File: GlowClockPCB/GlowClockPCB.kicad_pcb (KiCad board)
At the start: 2 copper layers, 102.9 x 64.8 mm, 30 parts, among them J1 LED_OUT_1, J2 LED_OUT_2, J3 LED_OUT_3, J4 LED_OUT_4, J5 POWER_IN, U1 RaspberryPi_Pico_W, U2 Raspberry_Pi_Zero_2_W, U3 DS3231MZ

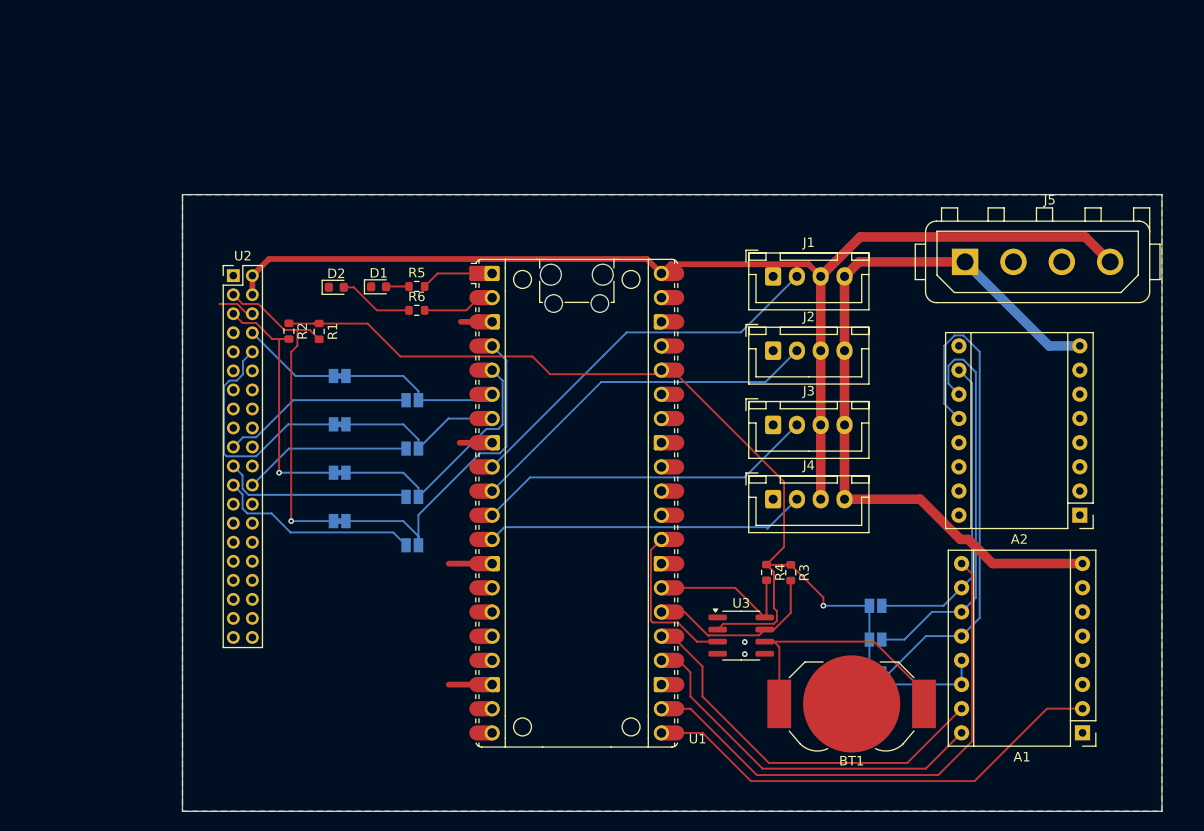
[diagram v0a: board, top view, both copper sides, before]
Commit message: add output connectors for motor drivers
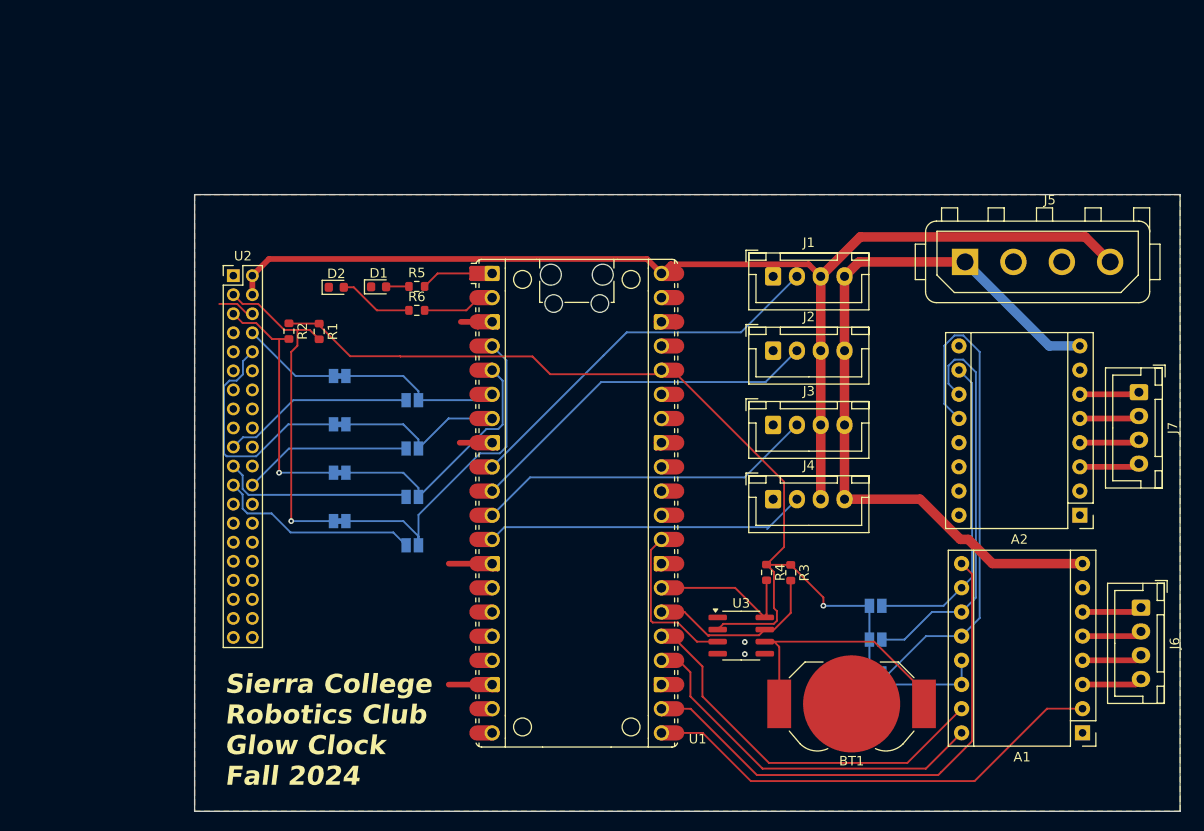
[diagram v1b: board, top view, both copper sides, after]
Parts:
- added J6: Motor_1_Out, Connector_JST:JST_XH_B4B-XH-A_1x04_P2.50mm_Vertical, F.Cu at (173.1, 156.4)
- added J7: Motor_2_Out, Connector_JST:JST_XH_B4B-XH-A_1x04_P2.50mm_Vertical, F.Cu at (172.8, 133.8)
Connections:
- A1 pad 3: unconnected-(A1-A2-Pad3) -> Net-(A1-A2)
- A1 pad 4: unconnected-(A1-A1-Pad4) -> Net-(A1-A1)
- A1 pad 5: unconnected-(A1-B1-Pad5) -> Net-(A1-B1)
- A1 pad 6: unconnected-(A1-B2-Pad6) -> Net-(A1-B2)
- A2 pad 3: unconnected-(A2-A2-Pad3) -> Net-(A2-A2)
- A2 pad 4: unconnected-(A2-A1-Pad4) -> Net-(A2-A1)
- A2 pad 5: unconnected-(A2-B1-Pad5) -> Net-(A2-B1)
- A2 pad 6: unconnected-(A2-B2-Pad6) -> Net-(A2-B2)
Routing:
- net Net-(A1-A2): track 0.00 -> 6.38 mm
- net Net-(A1-A1): track 0.00 -> 6.36 mm
- net Net-(A2-A2): track 0.00 -> 6.34 mm
- net Net-(A1-B1): track 0.00 -> 6.34 mm
- net Net-(A2-A1): track 0.00 -> 6.33 mm
- net Net-(A1-B2): track 0.00 -> 6.33 mm
- net Net-(A2-B1): track 0.00 -> 6.31 mm
- net Net-(A2-B2): track 0.00 -> 6.29 mm
- net +3V3: track 115.7 -> 115.2 mm
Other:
- board size 102.9 x 64.8 mm -> 103.5 x 64.8 mm
- board text added: "Sierra College Robotics Club Glow Clock Fall 2024"

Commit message: thicken high-current traces, and move text from silkscreen to copper layer
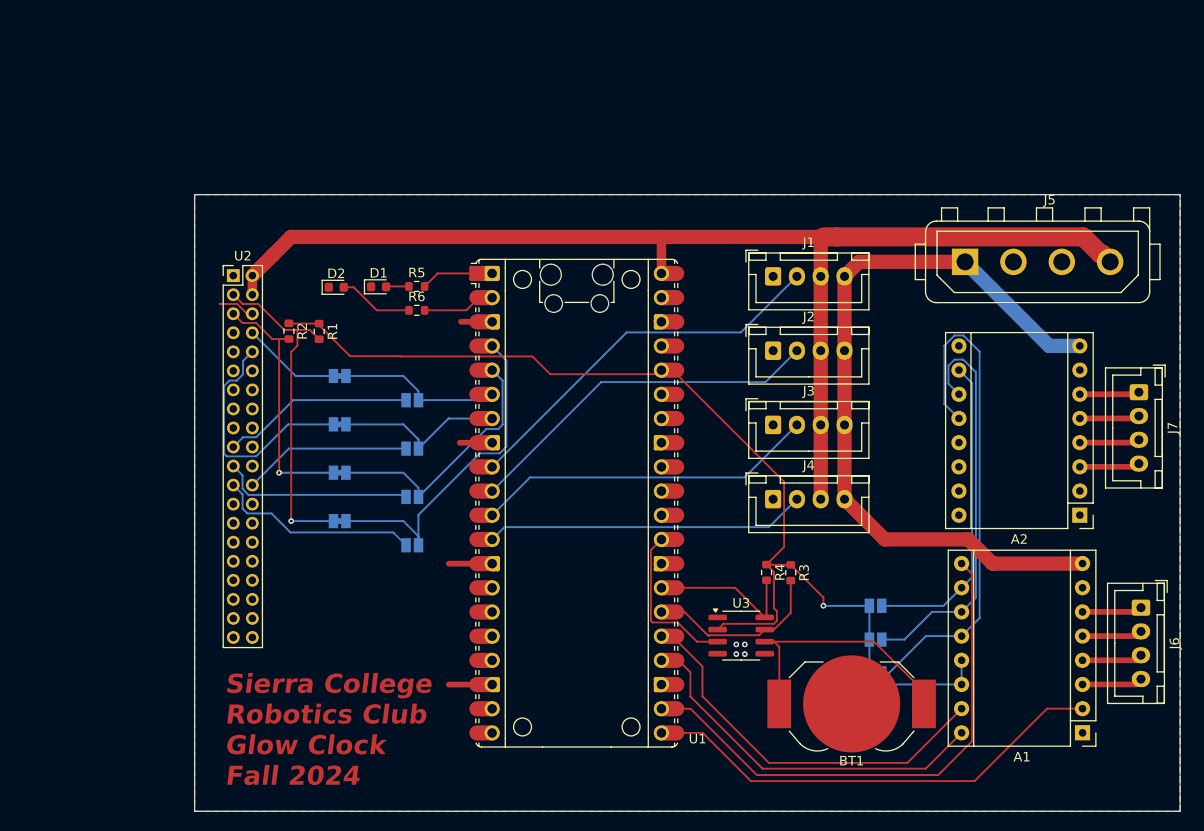
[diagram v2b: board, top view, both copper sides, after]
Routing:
- net +5V: track 120.6 -> 126.4 mm
- net GND: vias 2 -> 4
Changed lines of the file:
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@@
 		)
 		(property "Value" "StepperMode2"
-			(at 0 -1.9 0)
+			(at 0 -1.646 0)
 			(layer "B.SilkS")
 			(effects
@@
 	(gr_text "Sierra College\nRobotics Club\nGlow Clock\nFall 2024"
 		(at 76.835 175.26 0)
-		(layer "F.SilkS")
+		(layer "F.Cu")
+		(effects
+			(font
+				(size 2 2)
+				(thickness 0.3)
+				(bold yes)
+				(italic yes)
+			)
+			(justify left bottom)
+		)
+	)
+	(gr_text "Sierra College\nRobotics Club\nGlow Clock\nFall 2024"
+		(at 76.835 175.26 0)
+		(layer "F.Mask")
 		(effects
 			(font
@@
 	)
 	(via
-		(at 131.445 160.02)
+		(at 131.445 160.274)
+		(size 0.6)
+		(drill 0.3)
+		(layers "F.Cu" "B.Cu")
+		(free yes)
+		(net 1)
+	)
+	(via
+		(at 130.556 160.274)
+		(size 0.6)
+		(drill 0.3)
+		(layers "F.Cu" "B.Cu")
+		(free yes)
+		(net 1)
+	)
+	(via
+		(at 130.556 161.29)
 		(size 0.6)
 		(drill 0.3)
@@
 	)
 	(segment
-		(start 79.725 121.54)
-		(end 79.725 123.54)
-		(width 0.6)
+		(start 139.7 117.475)
+		(end 122.555 117.475)
+		(width 1.5)
 		(layer "F.Cu")
 		(net 17)
 	)
 	(segment
-		(start 122.69 121.31)
-		(end 121.17 119.79)
-		(width 0.6)
+		(start 169.0075 119.2825)
+		(end 168.8125 119.2825)
+		(width 2)
 		(layer "F.Cu")
 		(net 17)
 	)
 	(segment
-		(start 169.82 120.095)
-		(end 167.2 117.475)
+		(start 79.725 123.54)
+		(end 79.725 121.54)
 		(width 1)
 		(layer "F.Cu")
@@
 	)
 	(segment
-		(start 81.475 119.79)
-		(end 79.725 121.54)
-		(width 0.6)
+		(start 168.8125 119.2825)
+		(end 167.005 117.475)
+		(width 2)
 		(layer "F.Cu")
 		(net 17)
 	)
 	(segment
-		(start 138.145 120.345)
-		(end 123.655 120.345)
-		(width 0.6)
+		(start 139.42 117.755)
+		(end 139.7 117.475)
+		(width 1.5)
 		(layer "F.Cu")
 		(net 17)
 	)
 	(segment
-		(start 143.565 117.475)
-		(end 139.42 121.62)
+		(start 83.79 117.475)
+		(end 81.885 119.38)
+		(width 1.5)
+		(layer "F.Cu")
+		(net 17)
+	)
+	(segment
+		(start 141.09 117.475)
+		(end 139.7 117.475)
+		(width 2)
+		(layer "F.Cu")
+		(net 17)
+	)
+	(segment
+		(start 122.69 117.61)
+		(end 122.555 117.475)
 		(width 1)
-		(layer "F.Cu")
-		(net 17)
-	)
-	(segment
-		(start 139.42 121.62)
-		(end 138.145 120.345)
-		(width 0.6)
 		(layer "F.Cu")
 		(net 17)
@@
 		(start 139.42 121.62)
 		(end 139.42 145.02)
+		(width 1.5)
+		(layer "F.Cu")
+		(net 17)
+	)
+	(segment
+		(start 81.885 119.38)
+		(end 79.725 121.54)
+		(width 1.5)
+		(layer "F.Cu")
+		(net 17)
+	)
+	(segment
+		(start 139.42 121.62)
+		(end 139.42 117.755)
+		(width 1.5)
+		(layer "F.Cu")
+		(net 17)
+	)
+	(segment
+		(start 167.005 117.475)
+		(end 141.09 117.475)
+		(width 2)
+		(layer "F.Cu")
+		(net 17)
+	)
+	(segment
+		(start 122.69 121.31)
+		(end 122.69 117.61)
 		(width 1)
 		(layer "F.Cu")
@@
 	)
 	(segment
-		(start 123.655 120.345)
-		(end 122.69 121.31)
-		(width 0.6)
+		(start 169.82 120.095)
+		(end 169.0075 119.2825)
+		(width 2)
 		(layer "F.Cu")
 		(net 17)
 	)
 	(segment
-		(start 121.17 119.79)
-		(end 81.475 119.79)
-		(width 0.6)
-		(layer "F.Cu")
-		(net 17)
-	)
-	(segment
-		(start 167.2 117.475)
-		(end 143.565 117.475)
-		(width 1)
+		(start 122.555 117.475)
+		(end 83.79 117.475)
+		(width 1.5)
 		(layer "F.Cu")
 		(net 17)
@@
 	)
 	(segment
-		(start 141.92 145.02)
-		(end 149.86 145.02)
-		(width 1)
-		(layer "F.Cu")
-		(net 74)
-	)
-	(segment
 		(start 143.445 120.095)
 		(end 141.92 121.62)
-		(width 1)
+		(width 1.5)
 		(layer "F.Cu")
 		(net 74)
 	)
 	(segment
+		(start 166.915 151.78)
+		(end 157.459365 151.78)
+		(width 1.5)
+		(layer "F.Cu")
+		(net 74)
+	)
+	(segment
+		(start 146.142818 149.242818)
+		(end 141.92 145.02)
+		(width 1.5)
+		(layer "F.Cu")
+		(net 74)
+	)
+	(segment
 		(start 154.922182 149.242818)
-		(end 157.459365 151.78)
-		(width 1)
-		(layer "F.Cu")
-		(net 74)
-	)
-	(segment
-		(start 154.082818 149.242818)
-		(end 154.922182 149.242818)
-		(width 1)
+		(end 146.142818 149.242818)
+		(width 1.5)
 		(layer "F.Cu")
 		(net 74)
@@
 		(start 141.92 121.62)
 		(end 141.92 145.02)
-		(width 1)
+		(width 1.5)
 		(layer "F.Cu")
 		(net 74)
@@
 		(start 154.58 120.095)
 		(end 143.445 120.095)
-		(width 1)
+		(width 1.5)
 		(layer "F.Cu")
 		(net 74)
 	)
 	(segment
-		(start 149.86 145.02)
-		(end 154.082818 149.242818)
-		(width 1)
-		(layer "F.Cu")
-		(net 74)
-	)
-	(segment
 		(start 157.459365 151.78)
-		(end 166.915 151.78)
-		(width 1)
+		(end 154.922182 149.242818)
+		(width 1.5)
 		(layer "F.Cu")
 		(net 74)
@@
 		(start 154.58 120.095)
 		(end 163.405 128.92)
-		(width 1)
+		(width 1.5)
 		(layer "B.Cu")
 		(net 74)
@@
 		(start 163.405 128.92)
 		(end 166.635 128.92)
-		(width 1)
+		(width 1.5)
 		(layer "B.Cu")
 		(net 74)
@@
 		(width 0.2)
 		(layer "B.Cu")
-		(net 76)
-	)
-	(segment
-		(start 133.79 148.15)
-		(end 133.985 147.955)
-		(width 0.2)
-		(layer "B.Cu")

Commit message: lots of tweaks to design, add display port, mounting holes, decoupling caps, etc
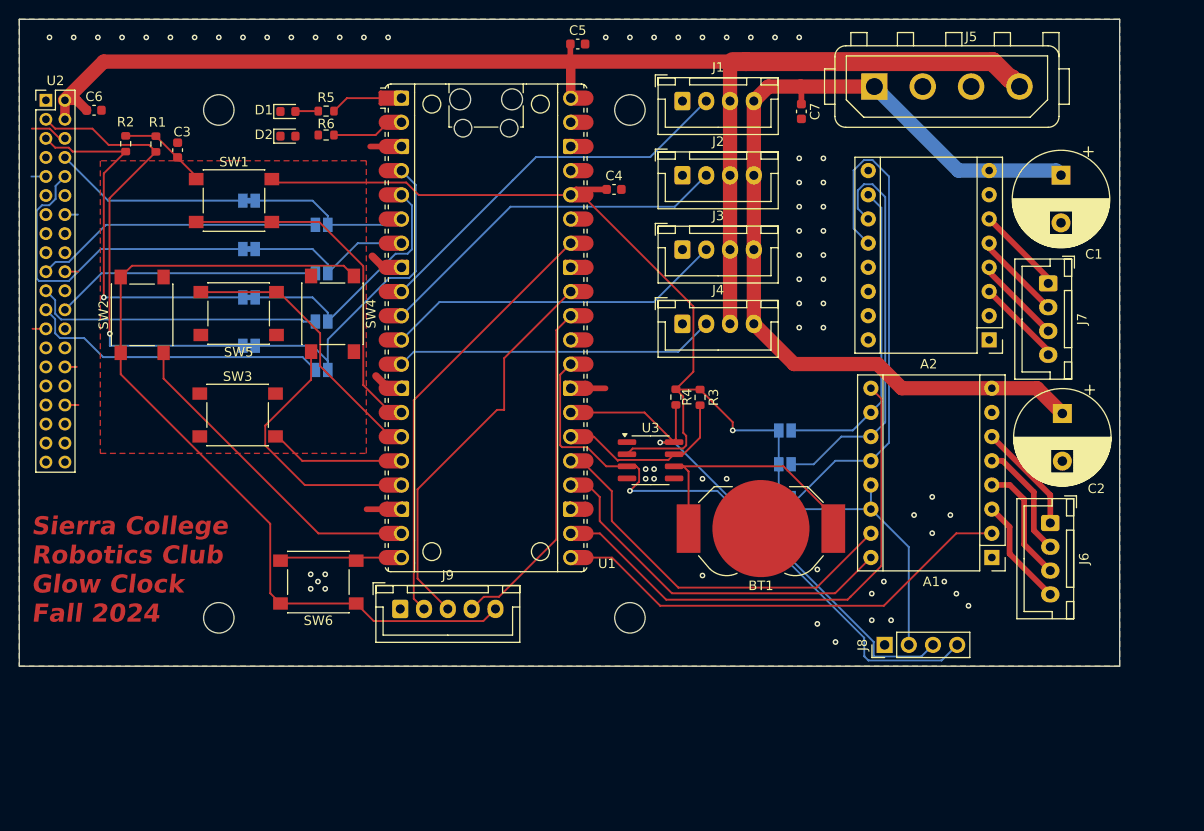
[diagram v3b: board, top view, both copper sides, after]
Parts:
- added C1: 100µF, Capacitor_THT:CP_Radial_D10.0mm_P5.00mm, F.Cu at (164.7, 111.0)
- added C2: 100µF, Capacitor_THT:CP_Radial_D10.0mm_P5.00mm, F.Cu at (164.8, 136.0)
- added C3: C, Capacitor_SMD:C_0603_1608Metric, F.Cu at (71.9, 108.3)
- added C4: C, Capacitor_SMD:C_0603_1608Metric, F.Cu at (117.7, 112.5)
- added C5: C, Capacitor_SMD:C_0603_1608Metric, F.Cu at (113.9, 97.2)
- added C6: C, Capacitor_SMD:C_0603_1608Metric, F.Cu at (63.1, 104.2)
- added C7: C, Capacitor_SMD:C_0603_1608Metric, F.Cu at (137.4, 104.3)
- added H1: MountingHole, MountingHole:MountingHole_3.2mm_M3, F.Cu at (76.2, 157.5)
- added H2: MountingHole, MountingHole:MountingHole_3.2mm_M3, F.Cu at (119.4, 157.5)
- added H3: MountingHole, MountingHole:MountingHole_3.2mm_M3, F.Cu at (119.4, 104.1)
- added H4: MountingHole, MountingHole:MountingHole_3.2mm_M3, F.Cu at (76.2, 104.1)
- added J8: I2C_LCD, Connector_PinHeader_2.54mm:PinHeader_1x04_P2.54mm_Vertical, F.Cu at (146.1, 160.3)
- added J9: ADC_OUT, Connector_JST:JST_XH_B5B-XH-A_1x05_P2.50mm_Vertical, F.Cu at (95.3, 156.5)
- added SW1: BTN_UP, Button_Switch_SMD:SW_Push_1P1T_NO_6x6mm_H9.5mm, F.Cu at (77.8, 113.7)
- added SW2: BTN_LEFT, Button_Switch_SMD:SW_Push_1P1T_NO_6x6mm_H9.5mm, F.Cu at (68.1, 125.7)
- added SW3: BTN_DOWN, Button_Switch_SMD:SW_Push_1P1T_NO_6x6mm_H9.5mm, F.Cu at (78.2, 136.2)
- added SW4: BTN_RIGHT, Button_Switch_SMD:SW_Push_1P1T_NO_6x6mm_H9.5mm, F.Cu at (88.1, 125.5)
- added SW5: BTN_OK, Button_Switch_SMD:SW_Push_1P1T_NO_6x6mm_H9.5mm, F.Cu at (78.3, 125.5)
- added SW6: BTN_BACK, Button_Switch_SMD:SW_Push_1P1T_NO_6x6mm_H9.5mm, F.Cu at (86.7, 153.7)
- moved U2 27.0 mm to (58.0, 103.1)
- moved R1 26.1 mm to (69.6, 107.7)
- moved R2 26.1 mm to (66.4, 107.7)
- moved BT1 20.7 mm to (133.1, 148.1)
- moved R3 20.7 mm to (126.7, 134.3)
- moved JP6 20.7 mm to (87.0, 131.4)
- moved R4 20.7 mm to (124.2, 134.3)
- moved D1 20.7 mm to (83.5, 104.3)
- moved JP1 20.7 mm to (79.4, 113.7)
- moved JP8 20.7 mm to (79.4, 123.8)
- moved R6 20.7 mm to (87.5, 106.8)
- moved J1 20.7 mm to (124.9, 103.2)
- moved J4 20.7 mm to (124.9, 126.6)
- moved JP4 20.7 mm to (87.0, 126.4)
- moved JP5 20.7 mm to (87.0, 116.2)
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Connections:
- U1 pad 14: unconnected-(U1-GPIO10-Pad14) -> Net-(U1-GPIO10)
- U1 pad 15: unconnected-(U1-GPIO11-Pad15) -> Net-(U1-GPIO11)
- U1 pad 16: unconnected-(U1-GPIO12-Pad16) -> Net-(U1-GPIO12)
- U1 pad 17: unconnected-(U1-GPIO13-Pad17) -> Net-(U1-GPIO13)
- U1 pad 19: unconnected-(U1-GPIO14-Pad19) -> Net-(U1-GPIO14)
- U1 pad 20: unconnected-(U1-GPIO15-Pad20) -> Net-(U1-GPIO15)
- U1 pad 31: unconnected-(U1-GPIO26_ADC0-Pad31) -> Net-(J9-Pin_4)
- U1 pad 32: unconnected-(U1-GPIO27_ADC1-Pad32) -> Net-(J9-Pin_3)
- U1 pad 34: unconnected-(U1-GPIO28_ADC2-Pad34) -> Net-(J9-Pin_2)
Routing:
- net +3V3: track 115.2 -> 226.2 mm
- net Net-(J8-Pin_4): track 16.9 -> 64.6 mm, vias 0 -> 1
- net Net-(J9-Pin_2): track 0.00 -> 45.7 mm
- net Net-(J9-Pin_3): track 0.00 -> 41.8 mm
- net Net-(J8-Pin_3): track 16.1 -> 56.9 mm, vias 0 -> 1
- net Net-(U1-GPIO10): track 0.00 -> 37.2 mm
- net Net-(J9-Pin_4): track 0.00 -> 36.0 mm
- net Net-(U1-GPIO14): track 0.00 -> 34.4 mm
- net Net-(U1-GPIO11): track 0.00 -> 29.1 mm
- net Net-(U1-GPIO13): track 0.00 -> 27.9 mm
- net +12V: track 80.2 -> 98.3 mm
- net +5V: track 126.4 -> 141.2 mm
- net Net-(U1-GPIO12): track 0.00 -> 14.0 mm
- net Net-(JP7-A): track 35.7 -> 49.3 mm
- net Net-(JP8-A): track 26.7 -> 39.8 mm
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- added copper zone on F.Cu, net +3V3
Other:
- board size 103.5 x 64.8 mm -> 115.6 x 67.9 mm

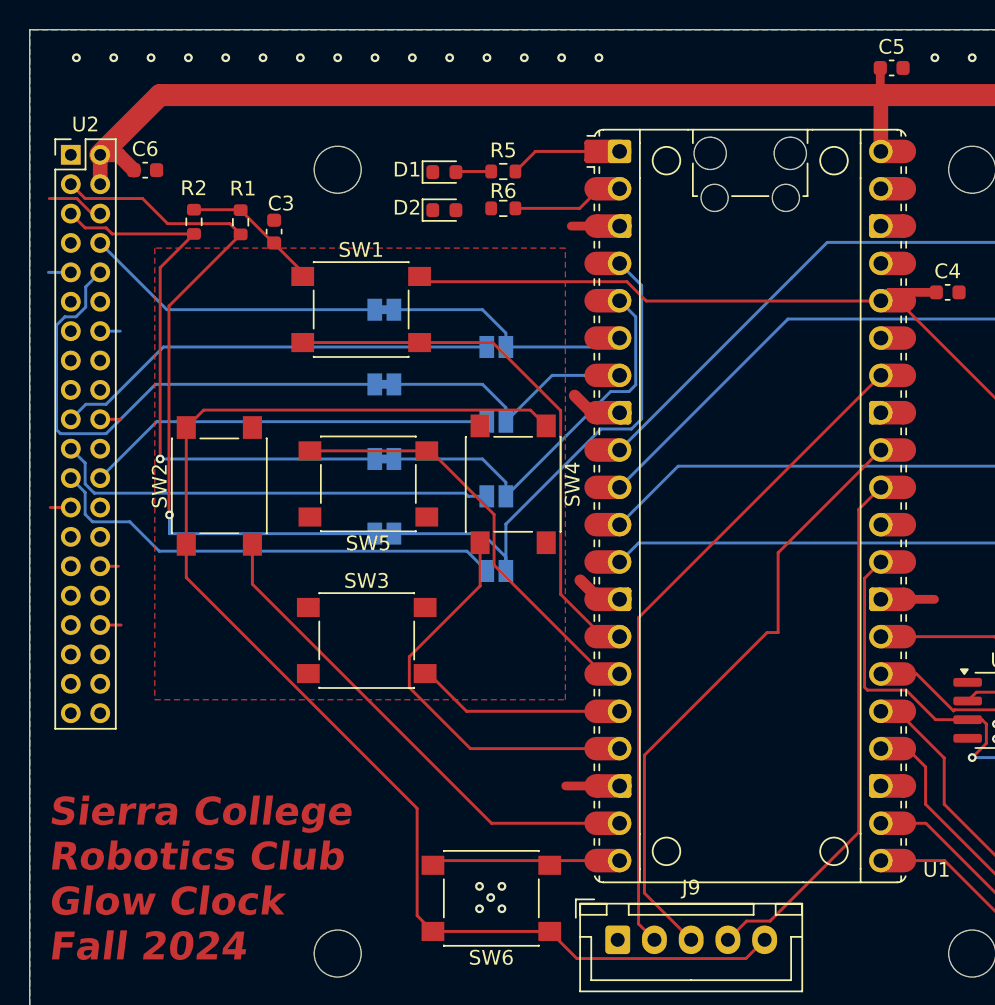
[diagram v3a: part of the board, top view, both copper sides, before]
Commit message: tweaks to resolve DRC errors
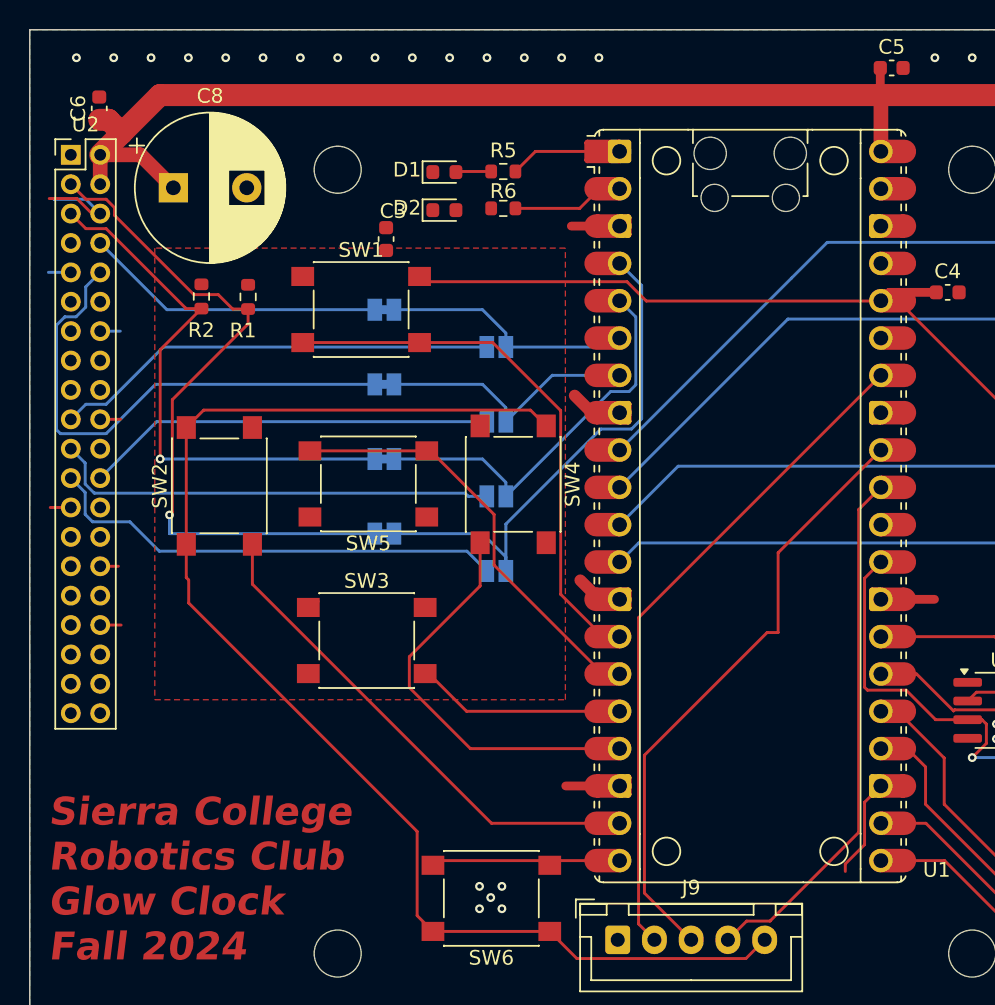
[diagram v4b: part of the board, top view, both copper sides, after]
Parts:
- added C8: 100µF, Capacitor_THT:CP_Radial_D10.0mm_P5.00mm, F.Cu at (65.0, 105.4)
- moved C3 7.64 mm to (79.5, 108.9)
- moved C6 5.24 mm to (60.0, 100.0), turned to 90 degrees
- moved R1 5.11 mm to (70.1, 112.8)
- moved R2 5.11 mm to (66.9, 112.8)
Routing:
- net GND: track 31.7 -> 42.1 mm
- net +3V3: track 226.2 -> 217.0 mm
- net +5V: track 141.2 -> 146.3 mm
- net Net-(JP8-A): track 39.8 -> 37.6 mm
- net Net-(JP7-A): track 49.3 -> 47.4 mm
